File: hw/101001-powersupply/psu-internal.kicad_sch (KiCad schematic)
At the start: 14 parts, among them U201 TPS54336ADDA

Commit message: Progress on board design
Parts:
- U201: footprint Package_SO:TI_SO-PowerPAD-8 -> Package_SO:TI_SO-PowerPAD-8_ThermalVias
- renumbered C207 to C206, C206 to C207
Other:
- company: (none) -> Sarif
- title: (none) -> Variable USB power supply
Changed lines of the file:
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@@
 	(generator_version "8.0")
 	(paper "A4")
+	(title_block
+		(title "Variable USB power supply")
+		(date "2024-04-23")
+		(rev "1")
+		(company "Sarif")
+	)
 	(junction
 		(at 143.51 129.54)
@@
 			)
 		)
-		(property "Footprint" "Package_SO:TI_SO-PowerPAD-8"
+		(property "Footprint" "Package_SO:TI_SO-PowerPAD-8_ThermalVias"
 			(at 168.91 102.87 0)
 			(effects
@@
 		(dnp no)
 		(fields_autoplaced yes)
-		(property "Reference" "#PWR0203"
+		(property "Reference" "#PWR0204"
 			(at 222.25 83.82 0)
 			(effects
@@
 			(project "101001-powersupply"
 				(path "/5b6c9e65-6d2e-4a49-a6e0-6edf7b37266c/355c0440-2bde-4095-9eb2-edbd94b04247"
-					(reference "#PWR0203")
+					(reference "#PWR0204")
 					(unit 1)
 				)
@@
 		(on_board yes)
 		(dnp no)
-		(property "Reference" "C207"
+		(property "Reference" "C206"
 			(at 205.74 104.14 90)
 			(effects
@@
 			(project "101001-powersupply"
 				(path "/5b6c9e65-6d2e-4a49-a6e0-6edf7b37266c/355c0440-2bde-4095-9eb2-edbd94b04247"
-					(reference "C207")
+					(reference "C206")
 					(unit 1)
 				)
@@
 		(dnp no)
 		(fields_autoplaced yes)
-		(property "Reference" "#PWR0204"
+		(property "Reference" "#PWR0203"
 			(at 135.89 181.61 0)
 			(effects
@@
 			(project "101001-powersupply"
 				(path "/5b6c9e65-6d2e-4a49-a6e0-6edf7b37266c/355c0440-2bde-4095-9eb2-edbd94b04247"
-					(reference "#PWR0204")
+					(reference "#PWR0203")
 					(unit 1)
 				)
@@
 		(on_board yes)
 		(dnp no)
-		(property "Reference" "C206"
+		(property "Reference" "C207"
 			(at 210.82 104.14 90)
 			(effects
@@
 			(project "101001-powersupply"
 				(path "/5b6c9e65-6d2e-4a49-a6e0-6edf7b37266c/355c0440-2bde-4095-9eb2-edbd94b04247"
-					(reference "C206")
+					(reference "C207")
 					(unit 1)
 				)

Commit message: Finalized board design
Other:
- note added: "AGND nettie near VCC capacitor ground"
- moved on the sheet: NT201
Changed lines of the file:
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@@
 	(wire
 		(pts
-			(xy 135.89 172.72) (xy 138.43 172.72)
+			(xy 137.16 177.8) (xy 139.7 177.8)
 		)
 		(stroke
@@
 	(wire
 		(pts
-			(xy 143.51 172.72) (xy 152.4 172.72)
+			(xy 144.78 177.8) (xy 153.67 177.8)
 		)
 		(stroke
@@
 	(wire
 		(pts
-			(xy 135.89 175.26) (xy 135.89 172.72)
+			(xy 137.16 180.34) (xy 137.16 177.8)
 		)
 		(stroke
@@
 			(width 0)
 			(type default)
+		)
+	)
+	(rectangle
+		(start 118.11 165.1)
+		(end 172.72 194.31)
+		(stroke
+			(width 0)
+			(type default)
+		)
+		(fill
+			(type none)
 		)
 	)
@@
 		)
 	)
+	(text "AGND nettie near VCC capacitor ground"
+		(exclude_from_sim no)
+		(at 119.38 193.04 0)
+		(effects
+			(font
+				(size 1.27 1.27)
+				(thickness 0.254)
+				(bold yes)
+			)
+			(justify left)
+		)
+	)
 	(label "AGND"
-		(at 152.4 172.72 180)
+		(at 153.67 177.8 180)
 		(fields_autoplaced yes)
 		(effects
@@
 	(symbol
 		(lib_id "power:GND")
-		(at 135.89 175.26 0)
+		(at 137.16 180.34 0)
 		(unit 1)
 		(exclude_from_sim no)
@@
 		(fields_autoplaced yes)
 		(property "Reference" "#PWR0203"
-			(at 135.89 181.61 0)
+			(at 137.16 186.69 0)
 			(effects
 				(font
@@
 		)
 		(property "Value" "GND"
-			(at 135.89 180.34 0)
+			(at 137.16 185.42 0)
 			(effects
 				(font
@@
 		)
 		(property "Footprint" ""
-			(at 135.89 175.26 0)
+			(at 137.16 180.34 0)
 			(effects
 				(font
@@
 		)
 		(property "Datasheet" ""
-			(at 135.89 175.26 0)
+			(at 137.16 180.34 0)
 			(effects
 				(font
@@
 		)
 		(property "Description" "Power symbol creates a global label with name \"GND\" , ground"
-			(at 135.89 175.26 0)
+			(at 137.16 180.34 0)
 			(effects
 				(font
@@
 	(symbol
 		(lib_id "Device:NetTie_2")
-		(at 140.97 172.72 0)
+		(at 142.24 177.8 0)
 		(unit 1)
 		(exclude_from_sim no)
@@
 		(fields_autoplaced yes)
 		(property "Reference" "NT201"
-			(at 140.97 167.64 0)
+			(at 142.24 172.72 0)
 			(effects
 				(font
@@
 		)
 		(property "Value" "NetTie_2"
-			(at 140.97 170.18 0)
+			(at 142.24 175.26 0)
 			(effects
 				(font
@@
 		)
 		(property "Footprint" "NetTie:NetTie-2_SMD_Pad0.5mm"
-			(at 140.97 172.72 0)
+			(at 142.24 177.8 0)
 			(effects
 				(font
@@
 		)
 		(property "Datasheet" "~"
-			(at 140.97 172.72 0)
+			(at 142.24 177.8 0)
 			(effects
 				(font
@@
 		)
 		(property "Description" "Net tie, 2 pins"
-			(at 140.97 172.72 0)
-			(effects
-				(font
+			(at 142.24 177.8 0)
+			(effects
+				(font

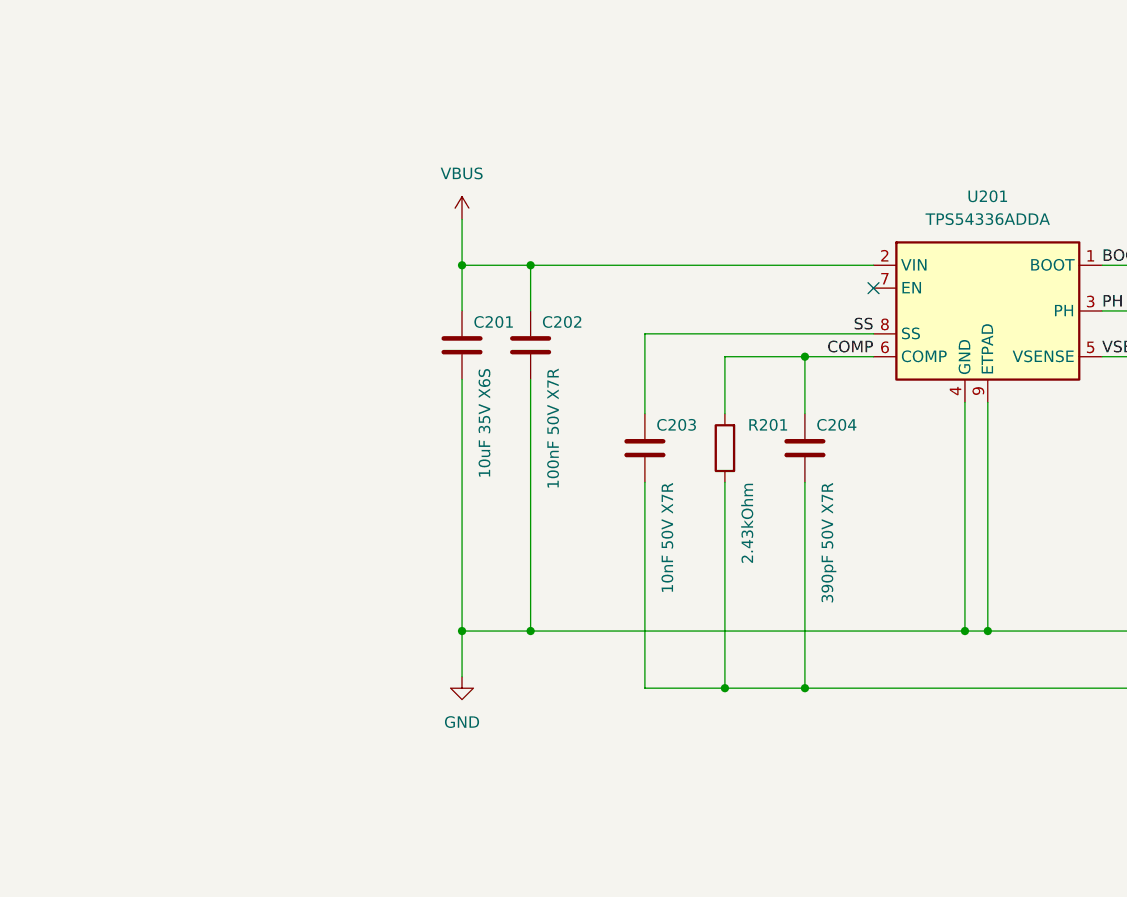
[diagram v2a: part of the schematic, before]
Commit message: Fixed Ccomp
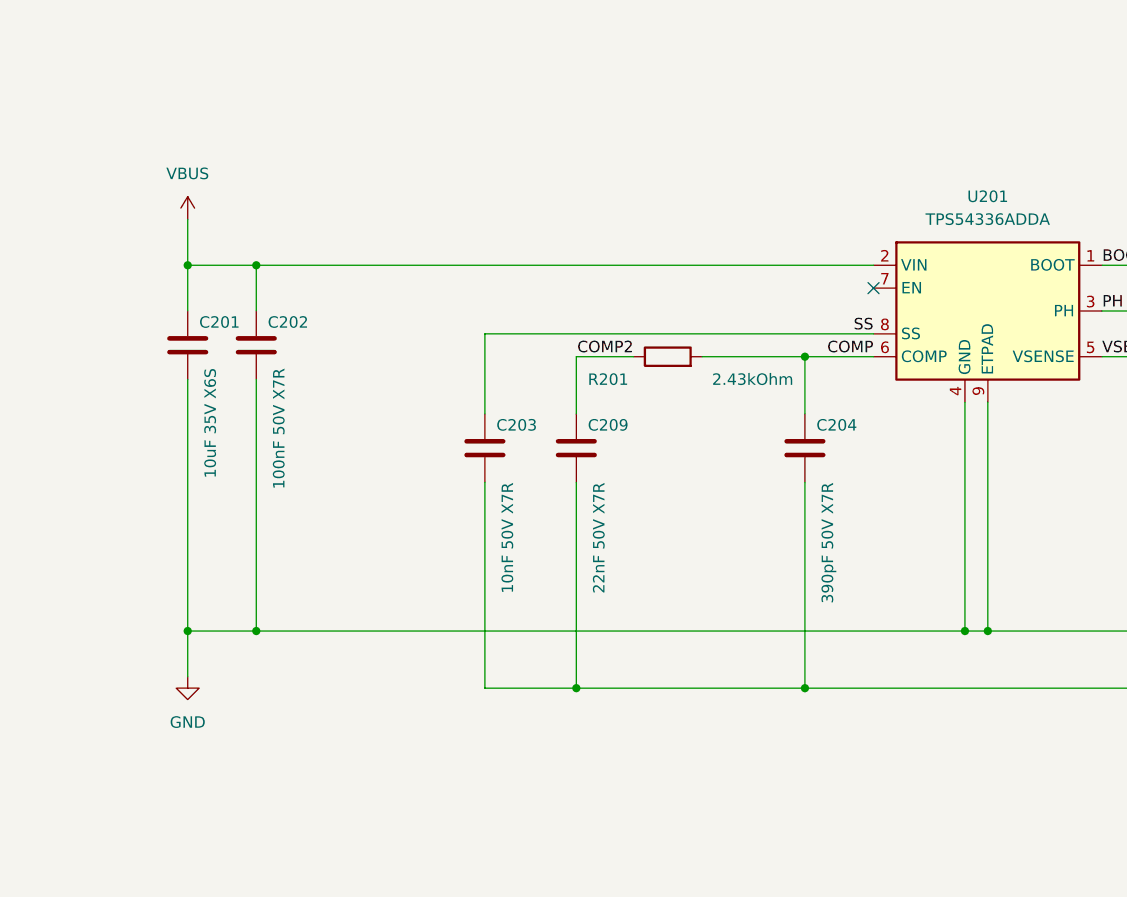
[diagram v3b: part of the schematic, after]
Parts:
- added C209: 22nF 50V X7R, Capacitor_SMD:C_0402_1005Metric, symbol Device:C
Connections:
- net AGND: now also C209.2; no longer R201.1
- new net COMP2: C209.1, R201.1
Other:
- moved on the sheet: C201, C202, C203, R201
